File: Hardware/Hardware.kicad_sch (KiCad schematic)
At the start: 0 parts

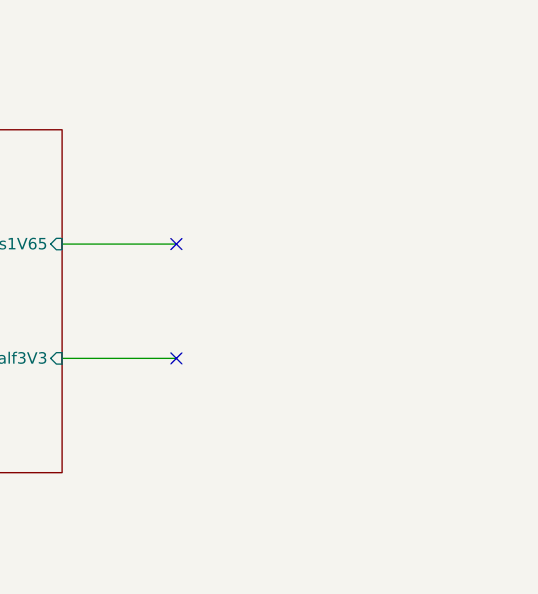
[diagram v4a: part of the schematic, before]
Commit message: made sheet MCU
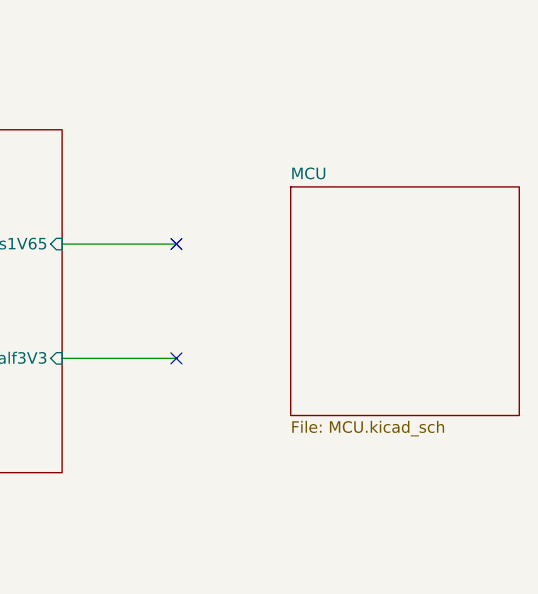
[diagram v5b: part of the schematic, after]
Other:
- added sheet MCU (MCU.kicad_sch)
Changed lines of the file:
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@@
+	)
+	(sheet
+		(at 190.5 101.6)
+		(size 25.4 25.4)
+		(fields_autoplaced yes)
+		(stroke
+			(width 0.1524)
+			(type solid)
+		)
+		(fill
+			(color 0 0 0 0.0000)
+		)
+		(property "Sheetname" "MCU"
+			(at 190.5 100.8884 0)
+			(effects
+				(font
+					(size 1.27 1.27)
+				)
+				(justify left bottom)
+			)
+		)
+		(property "Sheetfile" "MCU.kicad_sch"
+			(at 190.5 127.5846 0)
+			(effects
+				(font
+					(size 1.27 1.27)
+				)
+				(justify left top)
+			)
+		)
+		(instances
+			(project "Hardware"
+				(path "/4e457c11-25d4-4677-9942-6ed7396aaf8a"
+					(page "5")
+				)
+			)
+		)
 	)
 	(sheet

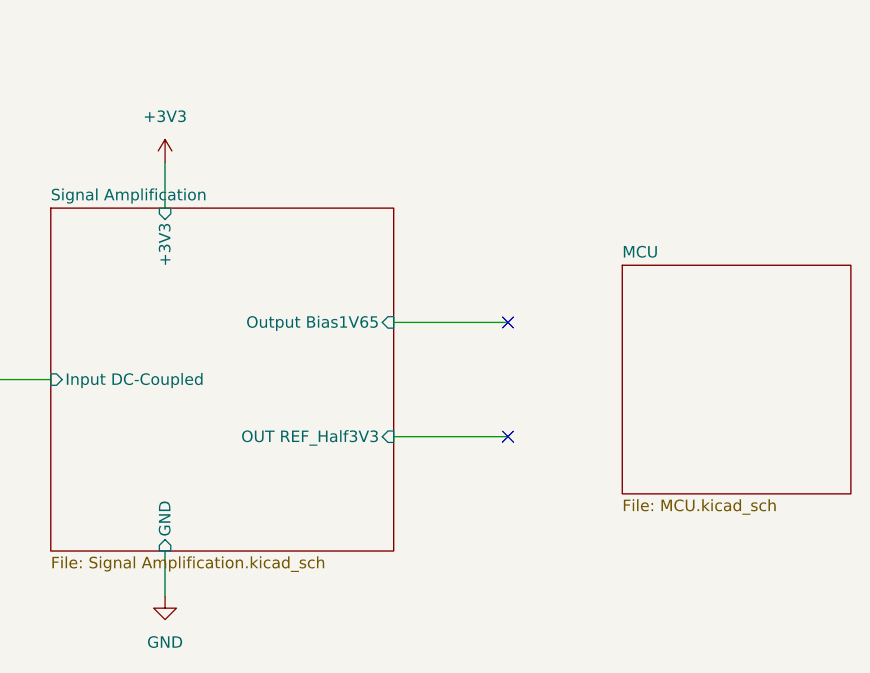
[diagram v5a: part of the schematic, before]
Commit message: Linked ampliefier sheet with mcu sheet
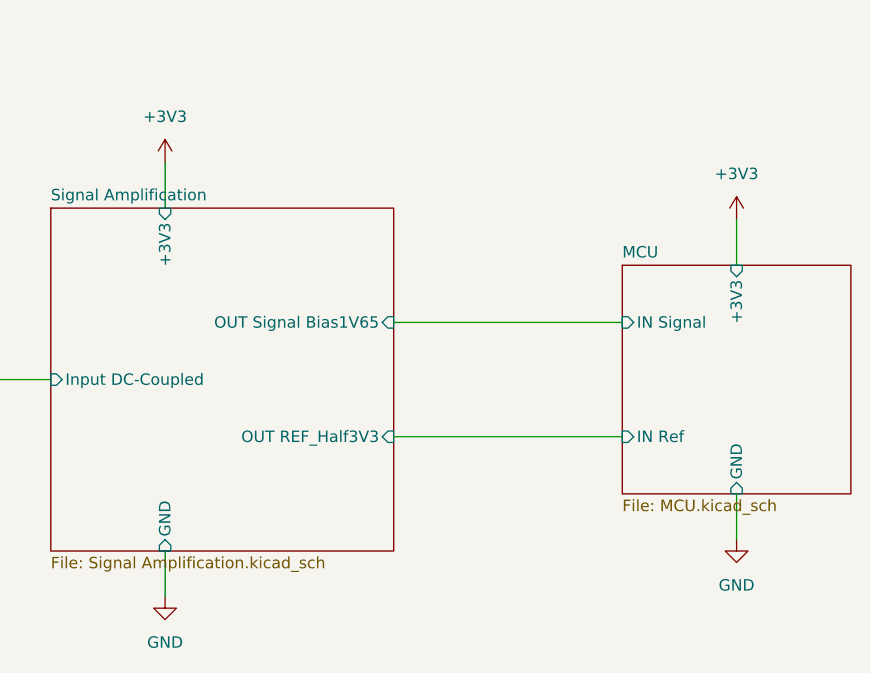
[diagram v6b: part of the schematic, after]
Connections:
- no-connect marks 2 -> 0
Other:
- sheet MCU ports: added +3V3, GND, IN Ref, IN Signal; removed none
- sheet Signal Amplification ports: added OUT Signal Bias1V65; removed Output Bias1V65
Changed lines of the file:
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@@
 	(generator_version "8.0")
 	(paper "A4")
-	(no_connect
-		(at 177.8 107.95)
-	)
-	(no_connect
-		(at 177.8 120.65)
-	)
 	(wire
 		(pts
@@
 	(wire
 		(pts
-			(xy 165.1 107.95) (xy 177.8 107.95)
+			(xy 165.1 107.95) (xy 190.5 107.95)
 		)
 		(stroke
@@
 	(wire
 		(pts
-			(xy 165.1 120.65) (xy 177.8 120.65)
+			(xy 165.1 120.65) (xy 190.5 120.65)
 		)
 		(stroke
@@
 	(wire
 		(pts
+			(xy 203.2 96.52) (xy 203.2 101.6)
+		)
+		(stroke
+			(width 0)
+			(type default)
+		)
+	)
+	(wire
+		(pts
 			(xy 143.51 59.69) (xy 143.51 64.77)
+		)
+		(stroke
+			(width 0)
+			(type default)
+		)
+	)
+	(wire
+		(pts
+			(xy 203.2 127) (xy 203.2 132.08)
 		)
 		(stroke
@@
 	)
 	(symbol
+		(lib_id "power:+3V3")
+		(at 203.2 96.52 0)
+		(unit 1)
+		(exclude_from_sim no)
+		(in_bom yes)
+		(on_board yes)
+		(dnp no)
+		(fields_autoplaced yes)
+		(property "Reference" "#PWR08"
+			(at 203.2 100.33 0)
+			(effects
+				(font
+					(size 1.27 1.27)
+				)
+				(hide yes)
+			)
+		)
+		(property "Value" "+3V3"
+			(at 203.2 91.44 0)
+			(effects
+				(font
+					(size 1.27 1.27)
+				)
+			)
+		)
+		(property "Footprint" ""
+			(at 203.2 96.52 0)
+			(effects
+				(font
+					(size 1.27 1.27)
+				)
+				(hide yes)
+			)
+		)
+		(property "Datasheet" ""
+			(at 203.2 96.52 0)
+			(effects
+				(font
+					(size 1.27 1.27)
+				)
+				(hide yes)
+			)
+		)
+		(property "Description" "Power symbol creates a global label with name \"+3V3\""
+			(at 203.2 96.52 0)
+			(effects
+				(font
+					(size 1.27 1.27)
+				)
+				(hide yes)
+			)
+		)
+		(pin "1"
+		)
+		(instances
+			(project "Hardware"
+				(path "/4e457c11-25d4-4677-9942-6ed7396aaf8a"
+					(reference "#PWR08")
+					(unit 1)
+				)
+			)
+		)
+	)
+	(symbol
+		(lib_id "power:GND")
+		(at 203.2 132.08 0)
+		(unit 1)
+		(exclude_from_sim no)
+		(in_bom yes)
+		(on_board yes)
+		(dnp no)
+		(fields_autoplaced yes)
+		(property "Reference" "#PWR09"
+			(at 203.2 138.43 0)
+			(effects
+				(font
+					(size 1.27 1.27)
+				)
+				(hide yes)
+			)
+		)
+		(property "Value" "GND"
+			(at 203.2 137.16 0)
+			(effects
+				(font
+					(size 1.27 1.27)
+				)
+			)
+		)
+		(property "Footprint" ""
+			(at 203.2 132.08 0)
+			(effects
+				(font
+					(size 1.27 1.27)
+				)
+				(hide yes)
+			)
+		)
+		(property "Datasheet" ""
+			(at 203.2 132.08 0)
+			(effects
+				(font
+					(size 1.27 1.27)
+				)
+				(hide yes)
+			)
+		)
+		(property "Description" "Power symbol creates a global label with name \"GND\" , ground"
+			(at 203.2 132.08 0)
+			(effects
+				(font
+					(size 1.27 1.27)
+				)
+				(hide yes)
+			)
+		)
+		(pin "1"
+		)
+		(instances
+			(project "Hardware"
+				(path "/4e457c11-25d4-4677-9942-6ed7396aaf8a"
+					(reference "#PWR09")
+					(unit 1)
+				)
+			)
+		)
+	)
+	(symbol
 		(lib_id "power:GND")
 		(at 139.7 138.43 0)
@@
 			)
 		)
+		(pin "GND" input
+			(at 203.2 127 270)
+			(effects
+				(font
+					(size 1.27 1.27)
+				)
+				(justify left)
+			)
+		)
+		(pin "+3V3" input
+			(at 203.2 101.6 90)
+			(effects
+				(font
+					(size 1.27 1.27)
+				)
+				(justify right)
+			)
+		)
+		(pin "IN Ref" input
+			(at 190.5 120.65 180)
+			(effects
+				(font
+					(size 1.27 1.27)
+				)
+				(justify left)
+			)
+		)
+		(pin "IN Signal" input
+			(at 190.5 107.95 180)
+			(effects
+				(font
+					(size 1.27 1.27)
+				)
+				(justify left)
+			)
+		)
 		(instances
 			(project "Hardware"
@@
 			)
 		)
-		(pin "Output Bias1V65" input
+		(pin "OUT Signal Bias1V65" input
 			(at 165.1 107.95 0)
 			(effects
